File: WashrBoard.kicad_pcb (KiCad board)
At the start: 2 copper layers, 70 x 50 mm, 38 parts, among them J1 TestPoint 5V, J10 ProgPoint GND, J2 USB_C_Receptacle_USB2.0_16P, J3 TestPoint GND, J4 TestPoint 3.3V, J5 JST GH, J6 ProgPoint 5V, J7 ProgPoint P9 GND, J8 ProgPointPoint D_P, J9 ProgPoint D_N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

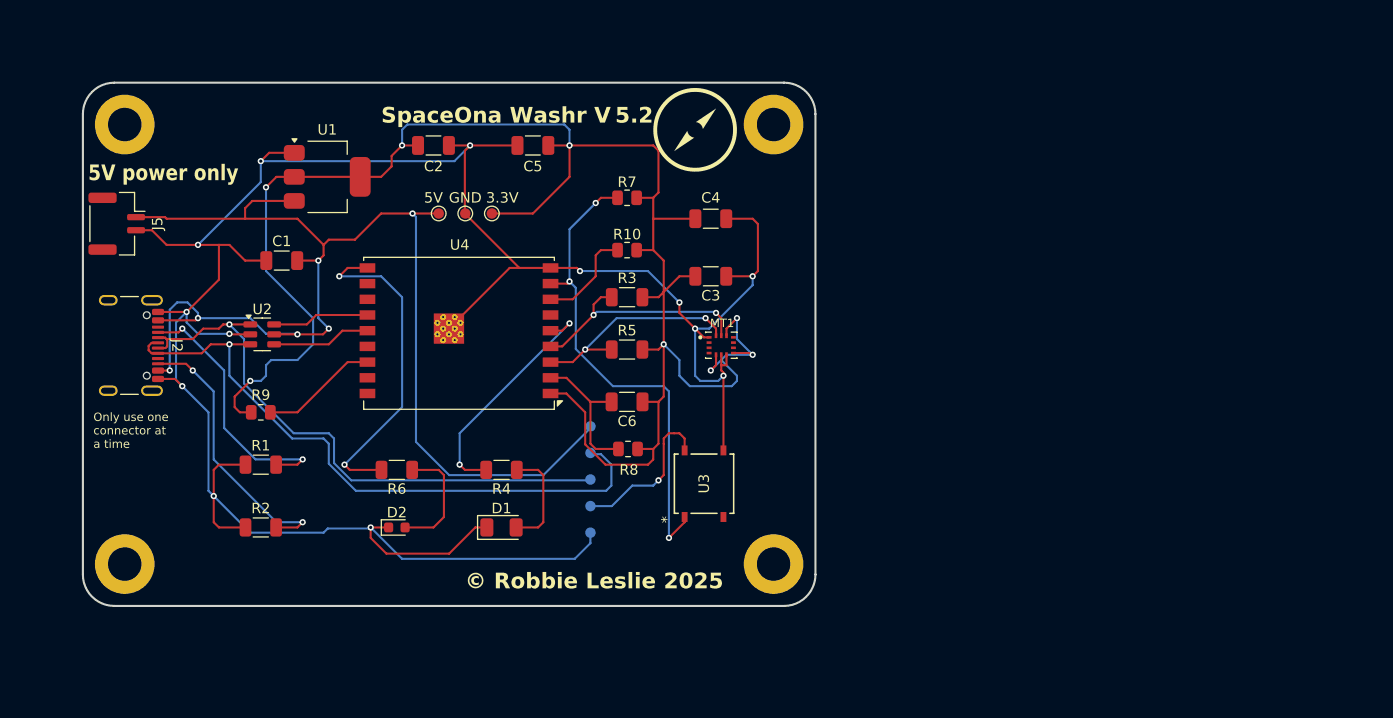
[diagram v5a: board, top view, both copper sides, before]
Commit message: Added fill zones
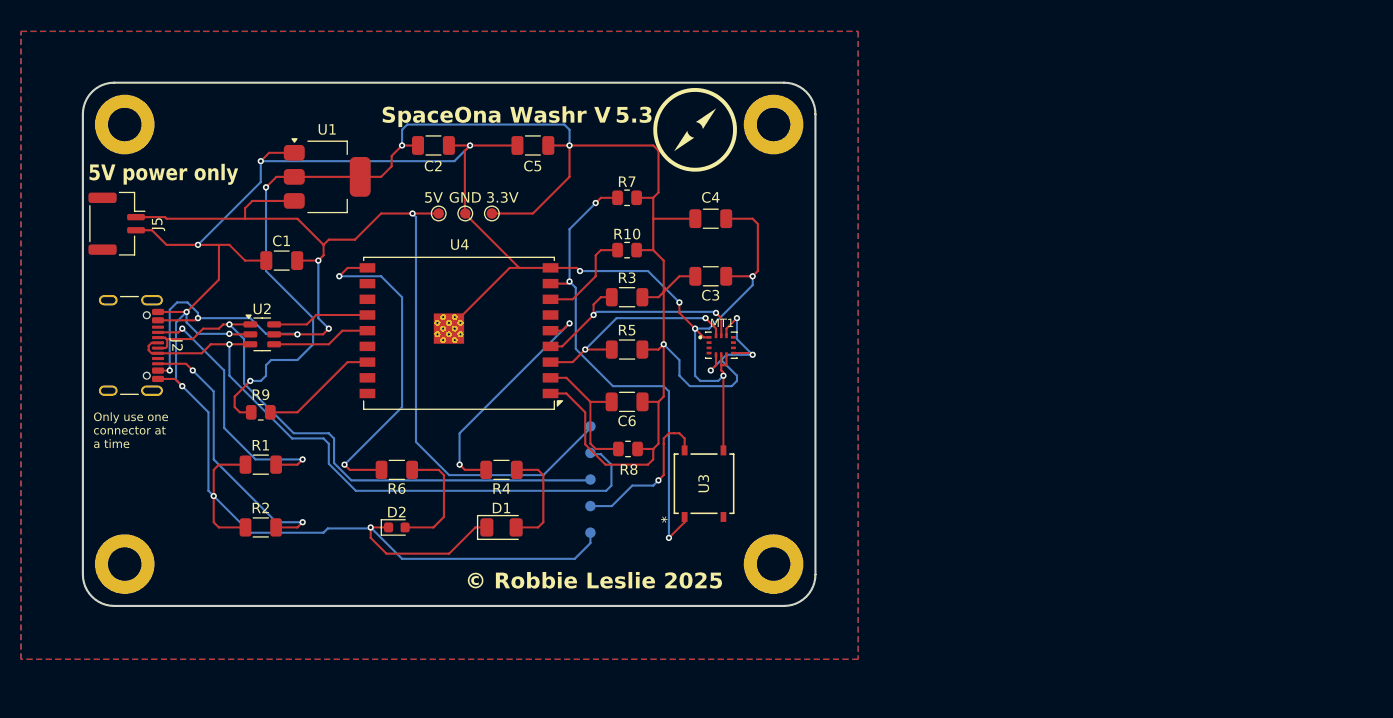
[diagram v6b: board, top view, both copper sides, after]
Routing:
- added copper zone on B.Cu, net GND
- added copper zone on F.Cu, net GND
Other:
- board text added: "2/2/2025"
- board text added: "SpaceOna Washr V 5.3"
- board text added: "V5.3"
- board text removed: "2/1/2025"
- board text removed: "SpaceOna Washr V 5.2"
- board text removed: "V5.2"
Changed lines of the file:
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@@
 		)
 	)
-	(gr_text "SpaceOna Washr V 5.2"
+	(gr_text "SpaceOna Washr V 5.3"
 		(at 95.42 35.4 0)
 		(layer "F.SilkS")
@@
 		)
 	)
-	(gr_text "2/1/2025"
+	(gr_text "2/2/2025"
 		(at 119 132 0)
 		(layer "Cmts.User")
@@
 		)
 	)
-	(gr_text "V5.2"
+	(gr_text "V5.3"
 		(at 181 132 0)
 		(layer "Cmts.User")
@@
 		(net 25)
 	)
+	(zone
+		(net 2)
+		(net_name "GND")
+		(layers "F&B.Cu")
+		(hatch edge 0.5)
+		(connect_pads
+			(clearance 0.5)
+		)
+		(min_thickness 0.25)
+		(filled_areas_thickness no)
+		(fill yes
+			(thermal_gap 0.5)
+			(thermal_bridge_width 0.5)
+		)
+		(polygon
+			(pts
+				(xy 61 26.5) (xy 141 26.5) (xy 141 86.5) (xy 61 86.5)
+			)
+		)
+	)
 )

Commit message: Added solder paste circle to mounting holes so they will be cut in the stencil
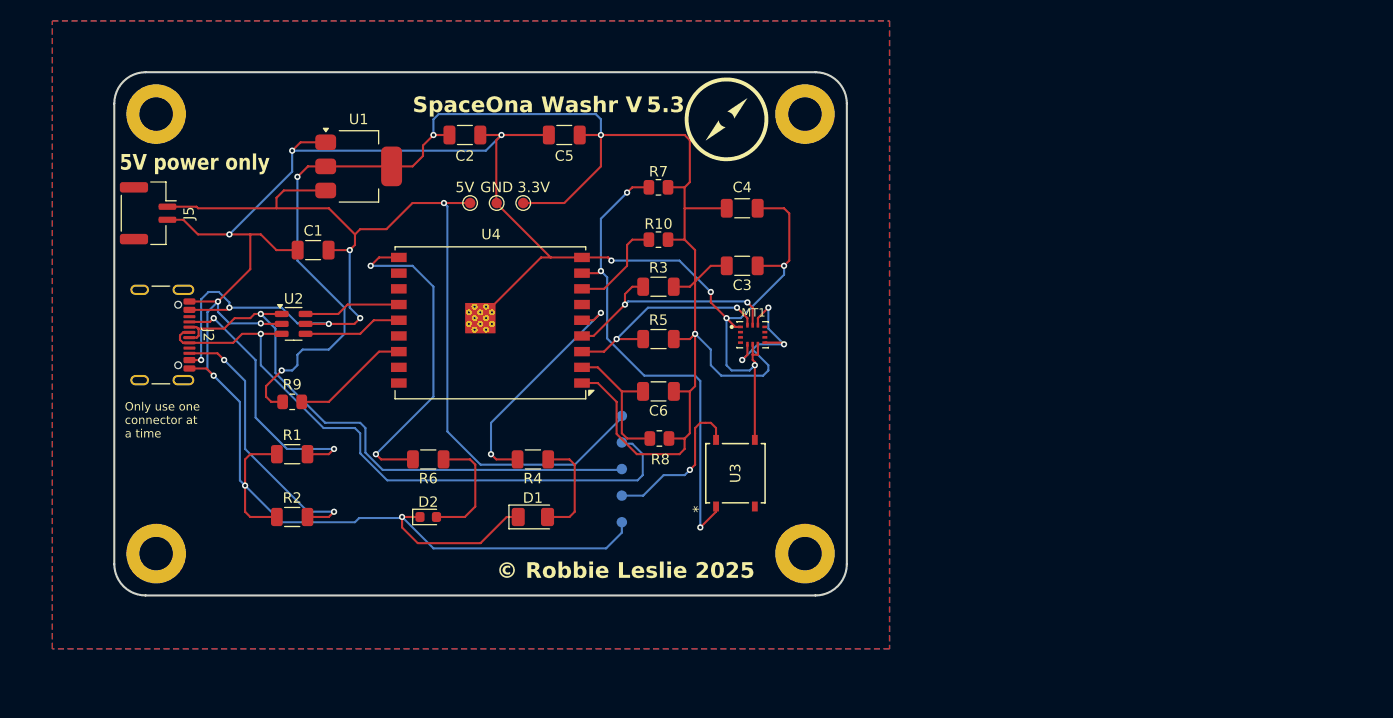
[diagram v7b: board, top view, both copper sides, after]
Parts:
- moved U3 3.16 mm to (129.3, 68.7)
- moved C1 3.16 mm to (88.9, 47.4)
- moved C2 3.16 mm to (103.4, 36.4)
- moved C5 3.16 mm to (112.9, 36.4)
- moved C6 3.16 mm to (121.9, 60.9)
- moved D1 3.16 mm to (109.9, 72.9)
- moved D2 3.16 mm to (99.9, 72.9)
- moved H1 3.16 mm to (73.9, 34.4)
- moved H2 3.16 mm to (135.9, 34.4)
- moved H3 3.16 mm to (73.9, 76.4)
- moved H4 3.16 mm to (135.9, 76.4)
- moved J1 3.16 mm to (103.9, 42.9)
- moved J10 3.16 mm to (118.4, 73.4)
- moved J2 3.16 mm to (73.4, 55.5)
- moved J3 3.16 mm to (106.5, 42.9)
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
